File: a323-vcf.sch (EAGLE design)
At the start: 105 parts, among them U1 SCREW-M2X8, U10 FX2-20S-1.27DS, U2 SCREW-M2X8, U3 NUT-M2-SELFLOCK, U4 NUT-M2-SELFLOCK, U5 FX2-20P-1.27DS, U6 SCREW-M2X8, U7 SCREW-M2X8, U8 NUT-M2-SELFLOCK, U9 NUT-M2-SELFLOCK

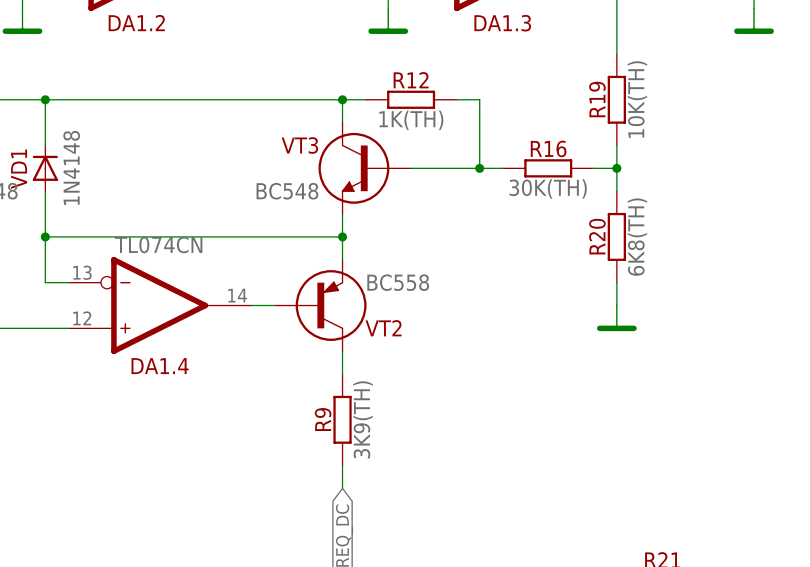
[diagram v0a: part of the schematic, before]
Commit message: BC558 -> BC556 Update
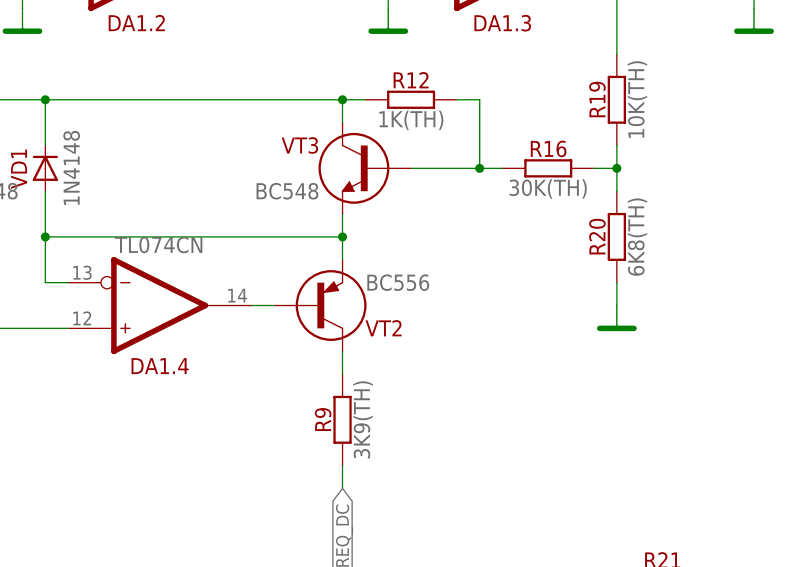
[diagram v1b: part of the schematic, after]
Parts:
- VT2: value BC558 -> BC556; device transistors-pnp:BC558 -> transistors-pnp:BC556
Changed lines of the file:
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@@
 <part name="R12" library="resistors" deviceset="?" device="1K(TH)"/>
 <part name="VT3" library="transistors-npn" deviceset="?" device="BC548"/>
-<part name="VT2" library="transistors-pnp" deviceset="?" device="BC558"/>
+<part name="VT2" library="transistors-pnp" deviceset="?" device="BC556"/>
 <part name="R9" library="resistors" deviceset="?" device="3K9(TH)"/>
 <part name="VD1" library="diodes" deviceset="?" device="1N4148"/>
